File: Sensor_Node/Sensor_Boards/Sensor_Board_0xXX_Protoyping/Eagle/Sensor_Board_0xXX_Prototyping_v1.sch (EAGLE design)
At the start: 24 parts, among them J1 M04_SMD_90, J4 ARDUINO_ISP, U2 ATMEGA328P_TQFP, Y1 8MHZ

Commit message: Finished SensorBoard Prototype
- minor changes
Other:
- note added: "Prototype Area"
- moved on the sheet: PAD1, PAD2, PAD3, PAD4, PAD5, PAD6, PAD7, PAD8, PAD9
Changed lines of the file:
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@@
 <setting verticaltext="up"/>
 </settings>
-<grid distance="0.1" unitdist="inch" unit="inch" style="lines" multiple="1" display="no" altdistance="0.01" altunitdist="inch" altunit="inch"/>
+<grid distance="0.1" unitdist="inch" unit="inch" style="lines" multiple="1" display="yes" altdistance="0.01" altunitdist="inch" altunit="inch"/>
 <layers>
 <layer number="1" name="Top" color="4" fill="1" visible="no" active="no"/>
@@
 <wire x1="104.14" y1="22.86" x2="104.14" y2="63.5" width="0.1524" layer="97" style="shortdash"/>
 <text x="55.118" y="60.452" size="1.778" layer="97">FTDI Pogopin Connector</text>
+<wire x1="172.72" y1="203.2" x2="129.54" y2="203.2" width="0.1524" layer="97" style="shortdash"/>
+<wire x1="129.54" y1="144.78" x2="129.54" y2="203.2" width="0.1524" layer="97" style="shortdash"/>
+<wire x1="172.72" y1="144.78" x2="172.72" y2="203.2" width="0.1524" layer="97" style="shortdash"/>
+<wire x1="172.72" y1="144.78" x2="129.54" y2="144.78" width="0.1524" layer="97" style="shortdash"/>
+<text x="132.08" y="198.12" size="1.778" layer="97">Prototype Area</text>
 </plain>
 <instances>
@@
 <instance part="P+6" gate="VCC" x="91.44" y="48.26"/>
 <instance part="C1" gate="G$1" x="30.48" y="182.88" rot="R90"/>
-<instance part="PAD1" gate="1" x="149.86" y="152.4" rot="R180"/>
-<instance part="U$1" gate="G$1" x="144.78" y="167.64"/>
-<instance part="PAD2" gate="1" x="149.86" y="147.32" rot="R180"/>
-<instance part="PAD3" gate="1" x="149.86" y="142.24" rot="R180"/>
-<instance part="PAD4" gate="1" x="149.86" y="137.16" rot="R180"/>
-<instance part="PAD5" gate="1" x="149.86" y="132.08" rot="R180"/>
-<instance part="PAD6" gate="1" x="149.86" y="127" rot="R180"/>
-<instance part="PAD7" gate="1" x="149.86" y="121.92" rot="R180"/>
-<instance part="PAD8" gate="1" x="149.86" y="116.84" rot="R180"/>
-<instance part="PAD9" gate="1" x="149.86" y="111.76" rot="R180"/>
+<instance part="PAD1" gate="1" x="134.62" y="193.04" rot="MR180"/>
+<instance part="U$1" gate="G$1" x="160.02" y="160.02"/>
+<instance part="PAD2" gate="1" x="134.62" y="187.96" rot="MR180"/>
+<instance part="PAD3" gate="1" x="134.62" y="182.88" rot="MR180"/>
+<instance part="PAD4" gate="1" x="134.62" y="177.8" rot="MR180"/>
+<instance part="PAD5" gate="1" x="134.62" y="172.72" rot="MR180"/>
+<instance part="PAD6" gate="1" x="134.62" y="167.64" rot="MR180"/>
+<instance part="PAD7" gate="1" x="134.62" y="162.56" rot="MR180"/>
+<instance part="PAD8" gate="1" x="134.62" y="157.48" rot="MR180"/>
+<instance part="PAD9" gate="1" x="134.62" y="152.4" rot="MR180"/>
 </instances>
 <busses>
@@
 </segment>
 <segment>
-<wire x1="147.32" y1="147.32" x2="142.24" y2="147.32" width="0.1524" layer="91"/>
-<label x="142.24" y="147.32" size="1.27" layer="95" rot="R180" xref="yes"/>
+<wire x1="137.16" y1="187.96" x2="142.24" y2="187.96" width="0.1524" layer="91"/>
+<label x="142.24" y="187.96" size="1.27" layer="95" rot="MR180" xref="yes"/>
 <pinref part="PAD2" gate="1" pin="P"/>
 </segment>
@@
 </segment>
 <segment>
-<wire x1="147.32" y1="152.4" x2="142.24" y2="152.4" width="0.1524" layer="91"/>
-<label x="142.24" y="152.4" size="1.27" layer="95" rot="R180" xref="yes"/>
+<wire x1="137.16" y1="193.04" x2="142.24" y2="193.04" width="0.1524" layer="91"/>
+<label x="142.24" y="193.04" size="1.27" layer="95" rot="MR180" xref="yes"/>
 <pinref part="PAD1" gate="1" pin="P"/>
 </segment>
@@
 </segment>
 <segment>
-<wire x1="147.32" y1="121.92" x2="142.24" y2="121.92" width="0.1524" layer="91"/>
-<label x="142.24" y="121.92" size="1.27" layer="95" rot="R180" xref="yes"/>
+<wire x1="137.16" y1="162.56" x2="142.24" y2="162.56" width="0.1524" layer="91"/>
+<label x="142.24" y="162.56" size="1.27" layer="95" rot="MR180" xref="yes"/>
 <pinref part="PAD7" gate="1" pin="P"/>
 </segment>
@@
 <net name="ADC6" class="0">
 <segment>
-<wire x1="147.32" y1="142.24" x2="142.24" y2="142.24" width="0.1524" layer="91"/>
-<label x="142.24" y="142.24" size="1.27" layer="95" rot="R180" xref="yes"/>
+<wire x1="137.16" y1="182.88" x2="142.24" y2="182.88" width="0.1524" layer="91"/>
+<label x="142.24" y="182.88" size="1.27" layer="95" rot="MR180" xref="yes"/>
 <pinref part="PAD3" gate="1" pin="P"/>
 </segment>
@@
 <net name="ADC7" class="0">
 <segment>
-<wire x1="147.32" y1="137.16" x2="142.24" y2="137.16" width="0.1524" layer="91"/>
-<label x="142.24" y="137.16" size="1.27" layer="95" rot="R180" xref="yes"/>
+<wire x1="137.16" y1="177.8" x2="142.24" y2="177.8" width="0.1524" layer="91"/>
+<label x="142.24" y="177.8" size="1.27" layer="95" rot="MR180" xref="yes"/>
 <pinref part="PAD4" gate="1" pin="P"/>
 </segment>
@@
 <net name="INT0" class="0">
 <segment>
-<wire x1="147.32" y1="132.08" x2="142.24" y2="132.08" width="0.1524" layer="91"/>
-<label x="142.24" y="132.08" size="1.27" layer="95" rot="R180" xref="yes"/>
+<wire x1="137.16" y1="172.72" x2="142.24" y2="172.72" width="0.1524" layer="91"/>
+<label x="142.24" y="172.72" size="1.27" layer="95" rot="MR180" xref="yes"/>
 <pinref part="PAD5" gate="1" pin="P"/>
 </segment>
@@
 <net name="INT1" class="0">
 <segment>
-<wire x1="147.32" y1="127" x2="142.24" y2="127" width="0.1524" layer="91"/>
-<label x="142.24" y="127" size="1.27" layer="95" rot="R180" xref="yes"/>
+<wire x1="137.16" y1="167.64" x2="142.24" y2="167.64" width="0.1524" layer="91"/>
+<label x="142.24" y="167.64" size="1.27" layer="95" rot="MR180" xref="yes"/>
 <pinref part="PAD6" gate="1" pin="P"/>
 </segment>
@@
 <net name="PC1" class="0">
 <segment>
-<wire x1="147.32" y1="116.84" x2="142.24" y2="116.84" width="0.1524" layer="91"/>
-<label x="142.24" y="116.84" size="1.27" layer="95" rot="R180" xref="yes"/>
+<wire x1="137.16" y1="157.48" x2="142.24" y2="157.48" width="0.1524" layer="91"/>
+<label x="142.24" y="157.48" size="1.27" layer="95" rot="MR180" xref="yes"/>
 <pinref part="PAD8" gate="1" pin="P"/>
 </segment>
@@
 <net name="PC2" class="0">
 <segment>
-<wire x1="147.32" y1="111.76" x2="142.24" y2="111.76" width="0.1524" layer="91"/>
-<label x="142.24" y="111.76" size="1.27" layer="95" rot="R180" xref="yes"/>
+<wire x1="137.16" y1="152.4" x2="142.24" y2="152.4" width="0.1524" layer="91"/>
+<label x="142.24" y="152.4" size="1.27" layer="95" rot="MR180" xref="yes"/>
 <pinref part="PAD9" gate="1" pin="P"/>
 </segment>

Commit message: Changed some SensorBoards
SHT31
- new routing

PULSE
- pogopin programmer now over FTDI
- interrupt to comboard now comes from atmega

TSL2561
- pogopin programmer now over FTDI

PROTOYPING
- changed title of schematic
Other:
- note added: "Sensor Board - Prototyping"
- note removed: "Sensor Board - SHT31"
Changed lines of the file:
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@@
 <setting verticaltext="up"/>
 </settings>
-<grid distance="0.1" unitdist="inch" unit="inch" style="lines" multiple="1" display="yes" altdistance="0.01" altunitdist="inch" altunit="inch"/>
+<grid distance="0.1" unitdist="inch" unit="inch" style="lines" multiple="1" display="no" altdistance="0.01" altunitdist="inch" altunit="inch"/>
 <layers>
 <layer number="1" name="Top" color="4" fill="1" visible="no" active="no"/>
@@
 <wire x1="47.752" y1="30.226" x2="7.62" y2="30.226" width="0.1524" layer="97" style="shortdash"/>
 <text x="8.89" y="60.071" size="1.778" layer="97">Communication Module Connector</text>
-<text x="224.527240625" y="11.421534375" size="2.54" layer="94" font="vector">Sensor Board - SHT31</text>
+<text x="224.527240625" y="11.421534375" size="2.54" layer="94" font="vector">Sensor Board - Prototyping</text>
 <text x="277.8550125" y="1.158059375" size="2.54" layer="94" font="vector">1.0</text>
 <wire x1="104.14" y1="63.5" x2="53.34" y2="63.5" width="0.1524" layer="97" style="shortdash"/>

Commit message: Updated schematic description
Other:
- note added: "Sensor Board - Prototyping (0xXX)"
- note removed: "Sensor Board - Prototyping"
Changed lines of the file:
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@@
 <wire x1="47.752" y1="30.226" x2="7.62" y2="30.226" width="0.1524" layer="97" style="shortdash"/>
 <text x="8.89" y="60.071" size="1.778" layer="97">Communication Module Connector</text>
-<text x="224.527240625" y="11.421534375" size="2.54" layer="94" font="vector">Sensor Board - Prototyping</text>
+<text x="224.527240625" y="11.421534375" size="2.54" layer="94" font="vector">Sensor Board - Prototyping (0xXX)</text>
 <text x="277.8550125" y="1.158059375" size="2.54" layer="94" font="vector">1.0</text>
 <wire x1="104.14" y1="63.5" x2="53.34" y2="63.5" width="0.1524" layer="97" style="shortdash"/>

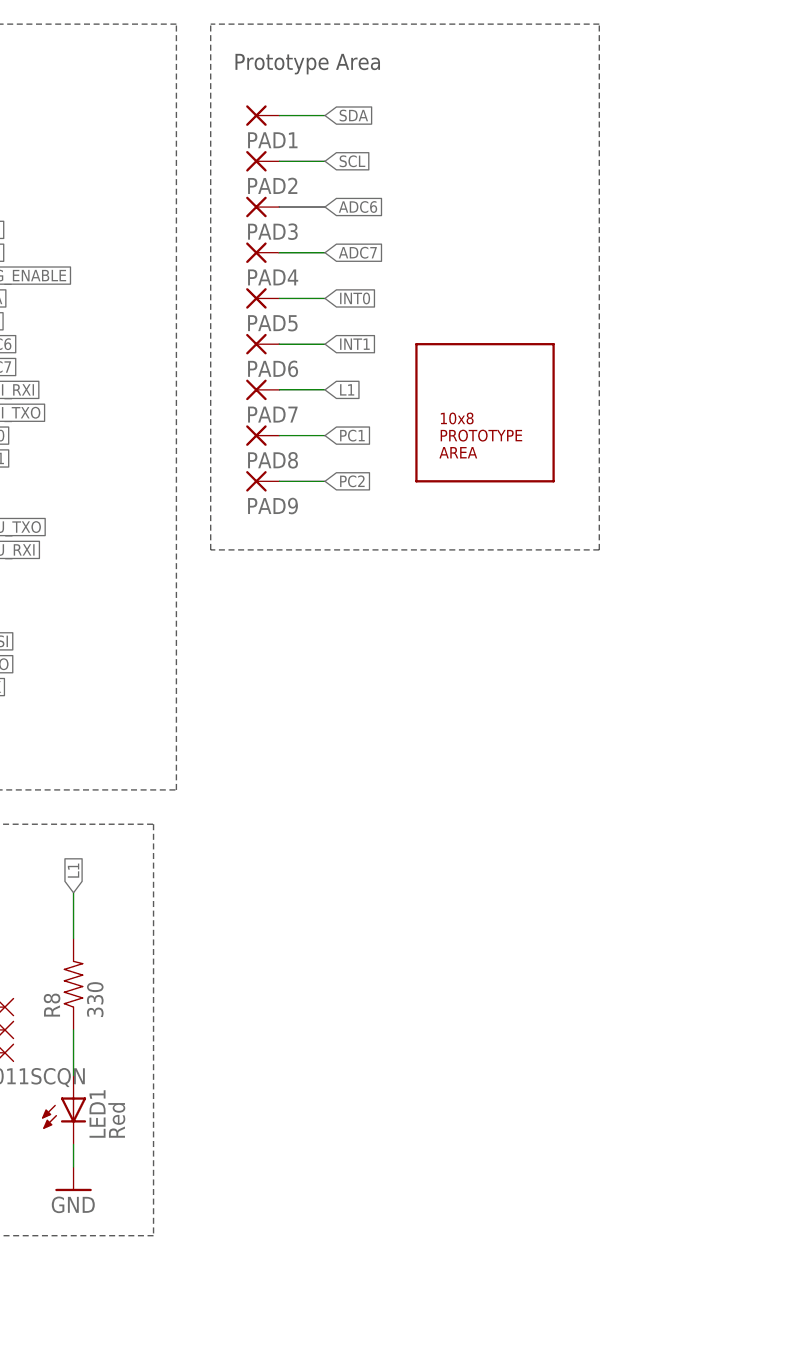
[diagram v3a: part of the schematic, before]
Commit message: Changes on Sensor Modules
- Finished SensModule-Prototype
- Changed some pin-descriptions on SensModule CO2
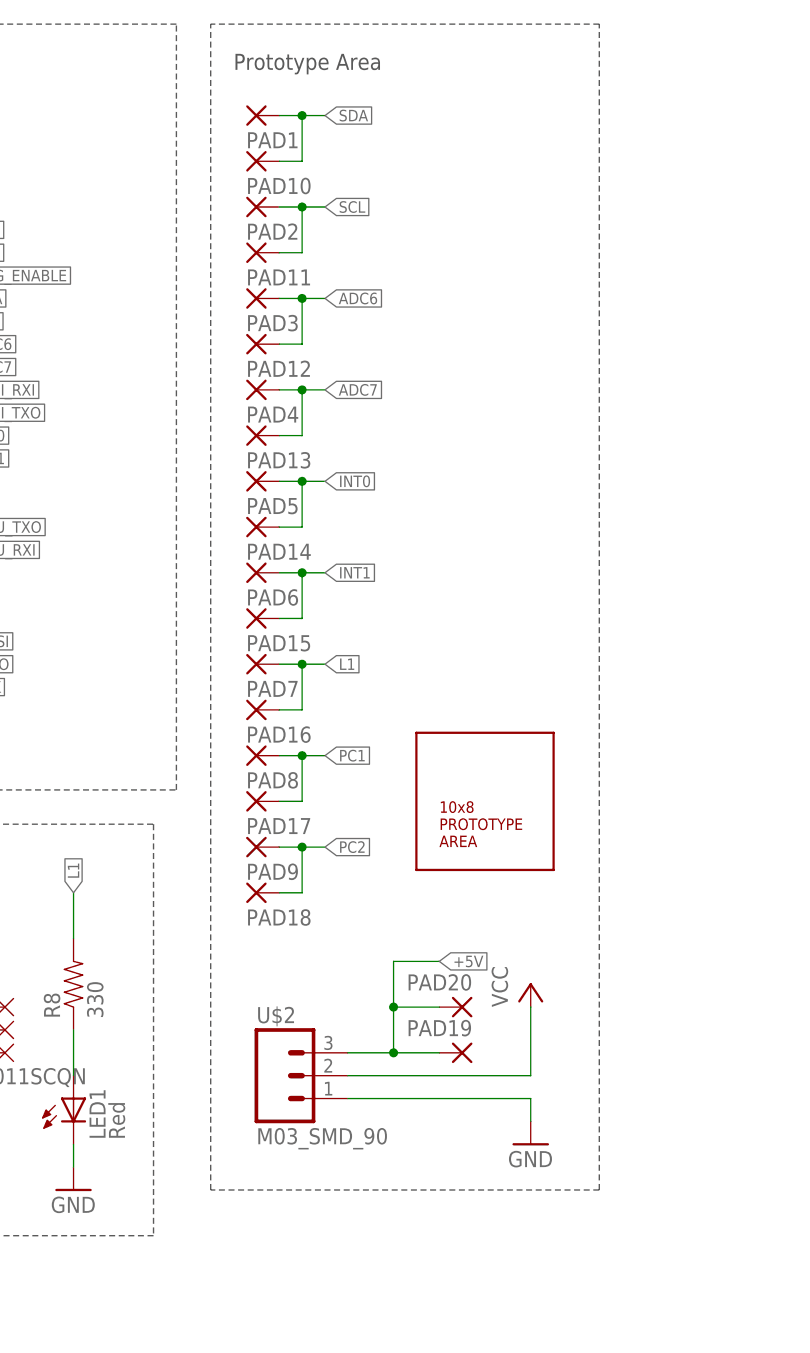
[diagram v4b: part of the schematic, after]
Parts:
- added PAD10, PAD11, PAD12, PAD13, PAD14, PAD15, PAD16, PAD17, PAD18, PAD19, PAD20: (no value), wirepad:1,6/0,9
- added U$2: M03_SMD_90, myownthings:M03_SMD_90
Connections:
- new net +5V: PAD19.P, PAD20.P, U$2.3
- net ADC6: now also PAD12.P
- net ADC7: now also PAD13.P
- net GND: now also U$2.1
- net INT0: now also PAD14.P
- net INT1: now also PAD15.P
- net L1: now also PAD16.P
- net PC1: now also PAD17.P
- net PC2: now also PAD18.P
- net SCL: now also PAD11.P
- net SDA: now also PAD10.P
- net VCC: now also U$2.2
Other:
- moved on the sheet: PAD2, PAD3, PAD4, PAD5, PAD6, PAD7, PAD8, PAD9
